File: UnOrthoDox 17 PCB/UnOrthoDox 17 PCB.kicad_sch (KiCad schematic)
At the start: 70 parts, among them SW1 SW_MX_HotSwap, SW10 SW_MX_HotSwap, SW11 SW_MX_HotSwap, SW12 SW_MX_HotSwap, SW13 SW_MX_HotSwap, SW14 SW_MX_HotSwap, SW15 SW_MX_HotSwap, SW16 SW_MX_HotSwap, SW17 SW_MX_HotSwap, SW18 SW_MX_HotSwap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

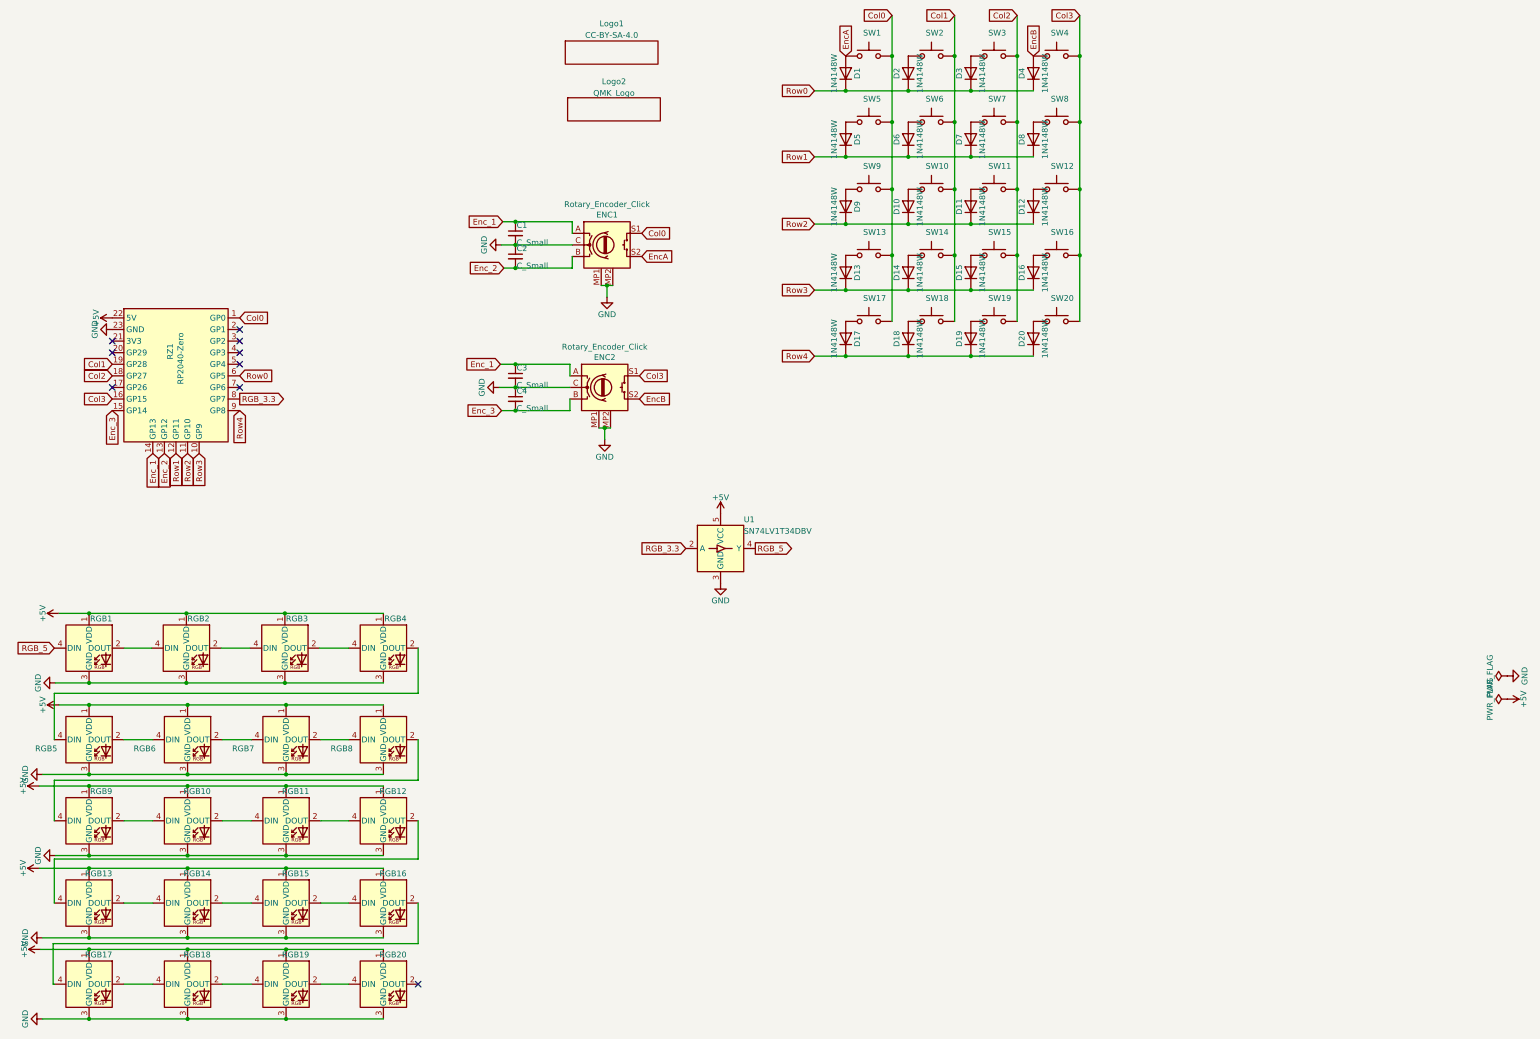
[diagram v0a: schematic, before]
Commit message: Final tweaks 17/20 PCB
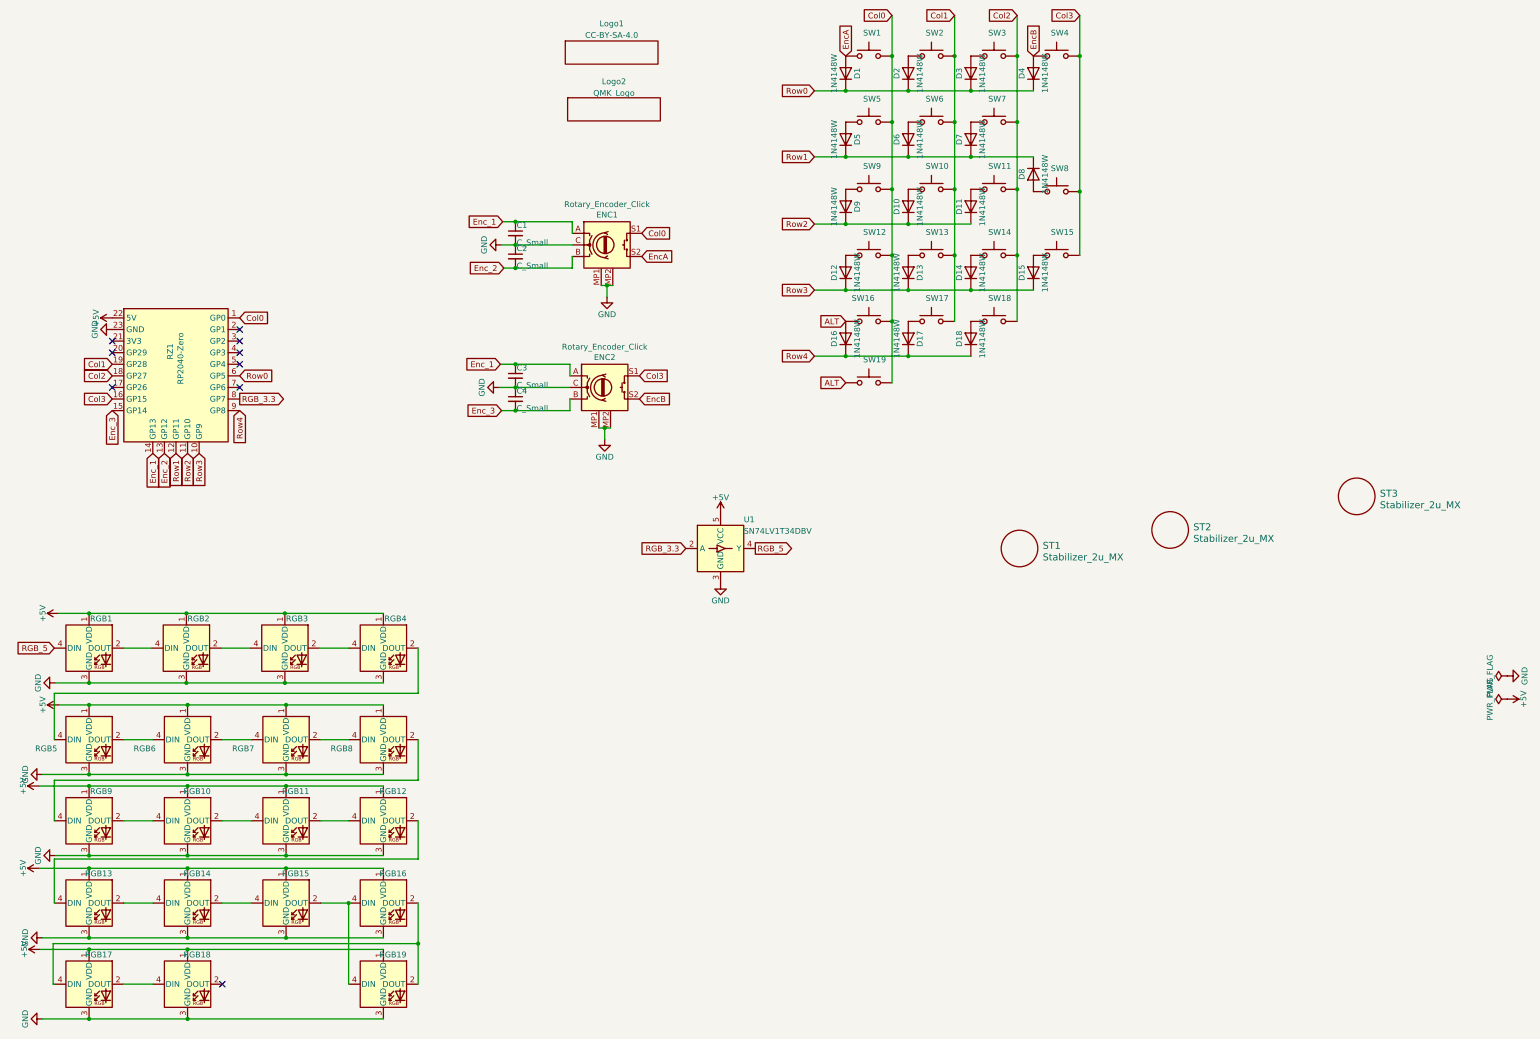
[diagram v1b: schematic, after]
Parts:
- removed D19, D20: 1N4148W, Diode_SMD:D_SOD-123, symbol Diode:1N4148W
- removed RGB20: SK6812MINI-E, Keyboard RGB:MX_SK6812MINI-E_REVERSIBLE, symbol Keyboard Common:SK6812MINI-E
- removed SW20: SW_MX_HotSwap, Keyboard Switches:SW_MX_HotSwap_Reversible, symbol Keyboard Switches:SW_MX_HotSwap
- added ST1, ST2, ST3: Stabilizer_2u_MX, Keyboard Stabilizer:Stabilizer_Cherry_MX_2.00u, symbol Keyboard Switches:Stabilizer_2u_MX
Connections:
- net Col0: now also SW12.2, SW16.1, SW19.2; no longer SW13.2, SW17.2
- net Col1: now also SW13.2, SW17.2; no longer SW14.2, SW18.2
- net Col2: now also SW14.2, SW18.2; no longer SW15.2, SW19.2
- net Col3: now also SW15.2; no longer SW12.2, SW16.2
- net Row2: no longer D12.1 (K)
- net Row3: now also D12.1 (K); no longer D16.1 (K)
- net Row4: now also D16.1 (K)
- net ALT: now reaches SW19.1
- net ALT: now also D16.2 (A), SW16.2
- net at RGB19.2 (DOUT): now also RGB16.2 (DOUT), RGB17.4 (DIN)
- net at RGB19.4 (DIN): now also RGB15.2 (DOUT), RGB16.4 (DIN); no longer RGB18.2 (DOUT)
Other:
- title: UnOrthoDox 20 -> UnOrthoDox 17
- moved on the sheet: D12, D13, D14, D15, D16, D17, D18, D8, SW12, SW13, SW14, SW15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
